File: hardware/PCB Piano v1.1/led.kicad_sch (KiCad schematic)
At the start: 46 parts, among them U4 PCA9685BS, U6 PCA9685BS

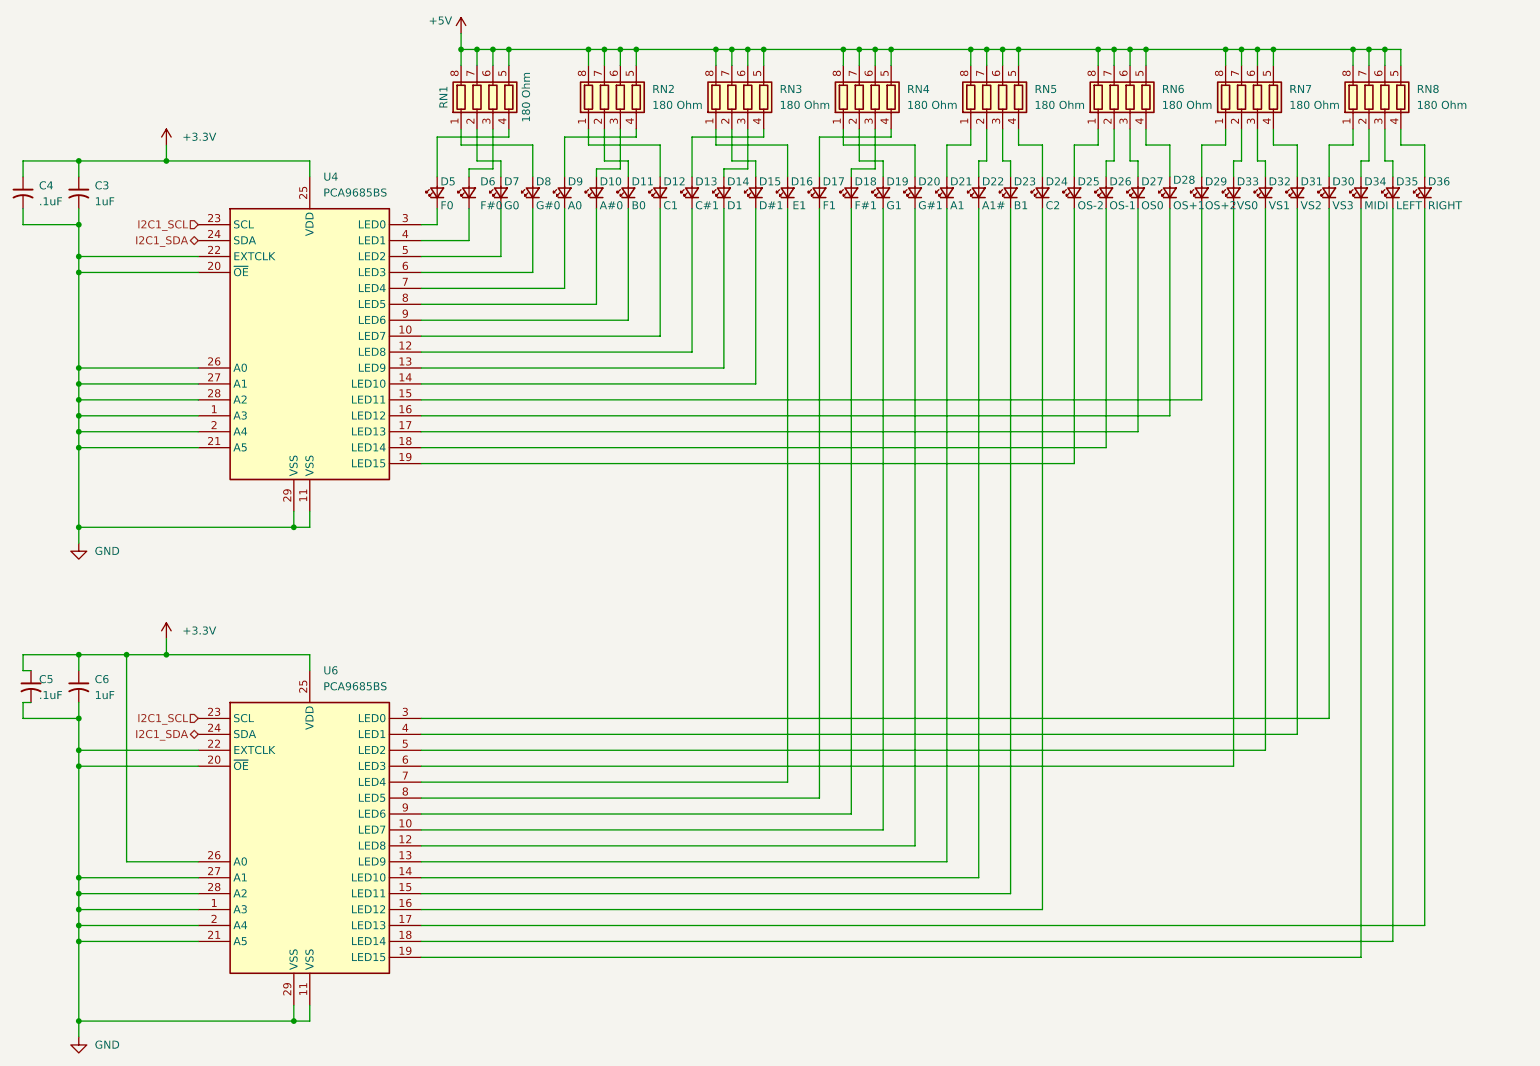
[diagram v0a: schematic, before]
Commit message: Firmware architecture complete - PCB revision with new charger.
Firmware Architecture Complete

- Added MP2724 charger driver
- Added TLV320DAC3100 driver
- Added MTCH2120 touch driver
- Added PCA9685 driver
- Added DotStar driver
- Added rotary encoder driver
- Added touch and LED maps
- Added control/audio/voice managers
- Added audio command queue
- Added Core1 audio architecture
- Added status LED system
- Added LED animation framework

Changes hardware schematic and PCB to accommodate a newer-style USB-C sink battery charger chip and USB data MUX to protect MCU while powered off.
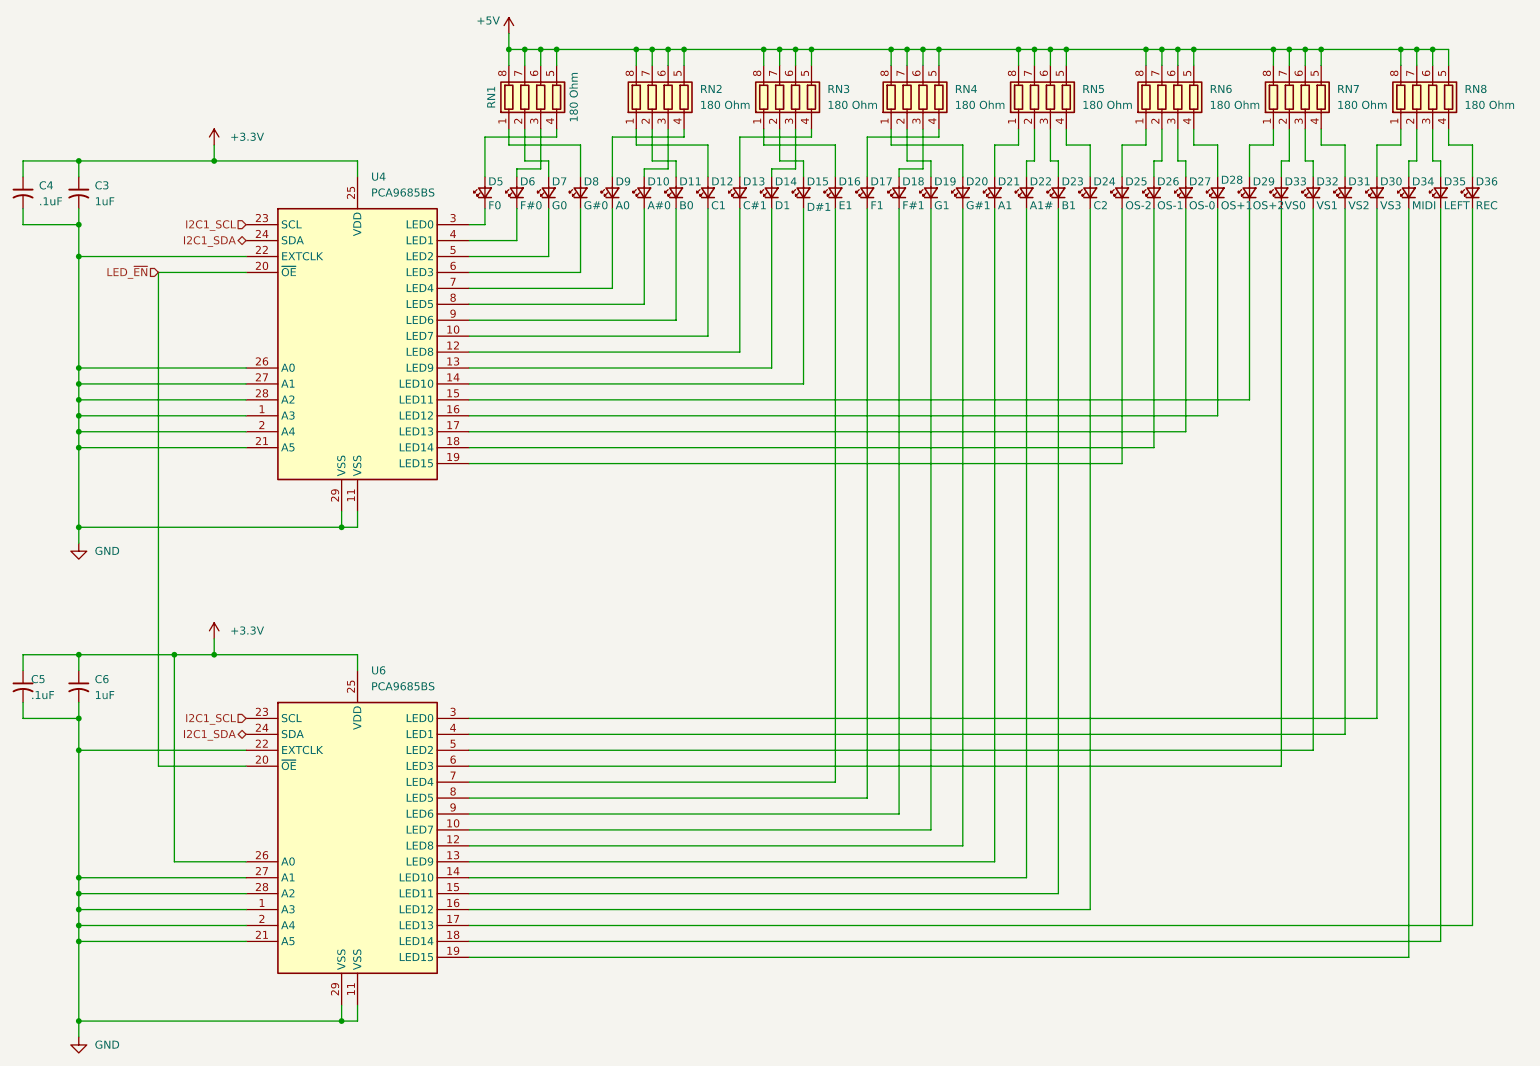
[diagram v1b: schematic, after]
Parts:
- D10: value A#0 -> LTST-C191TBKT; footprint LED_SMD:LED_0603_1608Metric -> PCBPiano_Footprints:LED_0603_1608Metric; Note (none) -> A#0
- D11: value B0 -> LTST-C191TBKT; footprint LED_SMD:LED_0603_1608Metric -> PCBPiano_Footprints:LED_0603_1608Metric; Note (none) -> B0
- D12: value C1 -> LTST-C191TBKT; footprint LED_SMD:LED_0603_1608Metric -> PCBPiano_Footprints:LED_0603_1608Metric; Note (none) -> C1
- D13: value C#1 -> LTST-C191TBKT; footprint LED_SMD:LED_0603_1608Metric -> PCBPiano_Footprints:LED_0603_1608Metric; Note (none) -> C#1
- D14: value D1 -> LTST-C191TBKT; footprint LED_SMD:LED_0603_1608Metric -> PCBPiano_Footprints:LED_0603_1608Metric; Note (none) -> D1
- D15: value D#1 -> LTST-C191TBKT; footprint LED_SMD:LED_0603_1608Metric -> PCBPiano_Footprints:LED_0603_1608Metric; Note (none) -> D#1
- D16: value E1 -> LTST-C191TBKT; footprint LED_SMD:LED_0603_1608Metric -> PCBPiano_Footprints:LED_0603_1608Metric; Note (none) -> E1
- D17: value F1 -> LTST-C191TBKT; footprint LED_SMD:LED_0603_1608Metric -> PCBPiano_Footprints:LED_0603_1608Metric; Note (none) -> F1
- D18: value F#1 -> LTST-C191TBKT; footprint LED_SMD:LED_0603_1608Metric -> PCBPiano_Footprints:LED_0603_1608Metric; Note (none) -> F#1
- D19: value G1 -> LTST-C191TBKT; footprint LED_SMD:LED_0603_1608Metric -> PCBPiano_Footprints:LED_0603_1608Metric; Note (none) -> G1
- D20: value G#1 -> LTST-C191TBKT; footprint LED_SMD:LED_0603_1608Metric -> PCBPiano_Footprints:LED_0603_1608Metric; Note (none) -> G#1
- D21: value A1 -> LTST-C191TBKT; footprint LED_SMD:LED_0603_1608Metric -> PCBPiano_Footprints:LED_0603_1608Metric; Note (none) -> A1
- D22: value A1# -> LTST-C191TBKT; footprint LED_SMD:LED_0603_1608Metric -> PCBPiano_Footprints:LED_0603_1608Metric; Note (none) -> A1#
- D23: value B1 -> LTST-C191TBKT; footprint LED_SMD:LED_0603_1608Metric -> PCBPiano_Footprints:LED_0603_1608Metric; Note (none) -> B1
- D24: value C2 -> LTST-C191TBKT; footprint LED_SMD:LED_0603_1608Metric -> PCBPiano_Footprints:LED_0603_1608Metric; Note (none) -> C2
- D25: value OS-2 -> LTST-C191TBKT; footprint LED_SMD:LED_0603_1608Metric -> PCBPiano_Footprints:LED_0603_1608Metric; Purpose (none) -> OS-2
- D26: value OS-1 -> LTST-C191TBKT; footprint LED_SMD:LED_0603_1608Metric -> PCBPiano_Footprints:LED_0603_1608Metric; Purpose (none) -> OS-1
- D27: value OS0 -> LTST-C191TBKT; footprint LED_SMD:LED_0603_1608Metric -> PCBPiano_Footprints:LED_0603_1608Metric; Purpose (none) -> OS-0
- D28: value OS+1 -> LTST-C191TBKT; footprint LED_SMD:LED_0603_1608Metric -> PCBPiano_Footprints:LED_0603_1608Metric; Purpose (none) -> OS+1
- D29: value OS+2 -> LTST-C191TBKT; footprint LED_SMD:LED_0603_1608Metric -> PCBPiano_Footprints:LED_0603_1608Metric; Purpose (none) -> OS+2
- D30: value VS3 -> LTST-C191TBKT; footprint LED_SMD:LED_0603_1608Metric -> PCBPiano_Footprints:LED_0603_1608Metric; Purpose (none) -> VS3
- D31: value VS2 -> LTST-C191TBKT; footprint LED_SMD:LED_0603_1608Metric -> PCBPiano_Footprints:LED_0603_1608Metric; Purpose (none) -> VS2
- D32: value VS1 -> LTST-C191TBKT; footprint LED_SMD:LED_0603_1608Metric -> PCBPiano_Footprints:LED_0603_1608Metric; Purpose (none) -> VS1
- D33: value VS0 -> LTST-C191TBKT; footprint LED_SMD:LED_0603_1608Metric -> PCBPiano_Footprints:LED_0603_1608Metric; Purpose (none) -> VS0
- D34: value MIDI -> LTST-C191TBKT; footprint LED_SMD:LED_0603_1608Metric -> PCBPiano_Footprints:LED_0603_1608Metric; Purpose (none) -> MIDI
- D35: value LEFT -> LTST-C191TBKT; footprint LED_SMD:LED_0603_1608Metric -> PCBPiano_Footprints:LED_0603_1608Metric; Purpose (none) -> LEFT
- D36: value RIGHT -> LTST-C191TBKT; footprint LED_SMD:LED_0603_1608Metric -> PCBPiano_Footprints:LED_0603_1608Metric; Purpose (none) -> REC
- D5: value F0 -> LTST-C191TBKT; footprint LED_SMD:LED_0603_1608Metric -> PCBPiano_Footprints:LED_0603_1608Metric; Note (none) -> F0
- D6: value F#0 -> LTST-C191TBKT; footprint LED_SMD:LED_0603_1608Metric -> PCBPiano_Footprints:LED_0603_1608Metric; Note (none) -> F#0
- D7: value G0 -> LTST-C191TBKT; footprint LED_SMD:LED_0603_1608Metric -> PCBPiano_Footprints:LED_0603_1608Metric; Note (none) -> G0
- D8: value G#0 -> LTST-C191TBKT; footprint LED_SMD:LED_0603_1608Metric -> PCBPiano_Footprints:LED_0603_1608Metric; Note (none) -> G#0
- D9: value A0 -> LTST-C191TBKT; footprint LED_SMD:LED_0603_1608Metric -> PCBPiano_Footprints:LED_0603_1608Metric; Note (none) -> A0
- RN1, RN2, RN3, RN4, RN5, RN6, RN7, RN8: footprint Resistor_SMD:R_Array_Convex_4x1206 -> PCBPiano_Footprints:R_Array_Convex_4x1206
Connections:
- net GND: no longer U4.20 (~{OE}), U6.20 (~{OE})
- new net LED_~{EN}: U4.20 (~{OE}), U6.20 (~{OE})
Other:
- moved on the sheet: C5, D10, D11, D12, D13, D14, D15, D16, D17, D18, D19, D20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

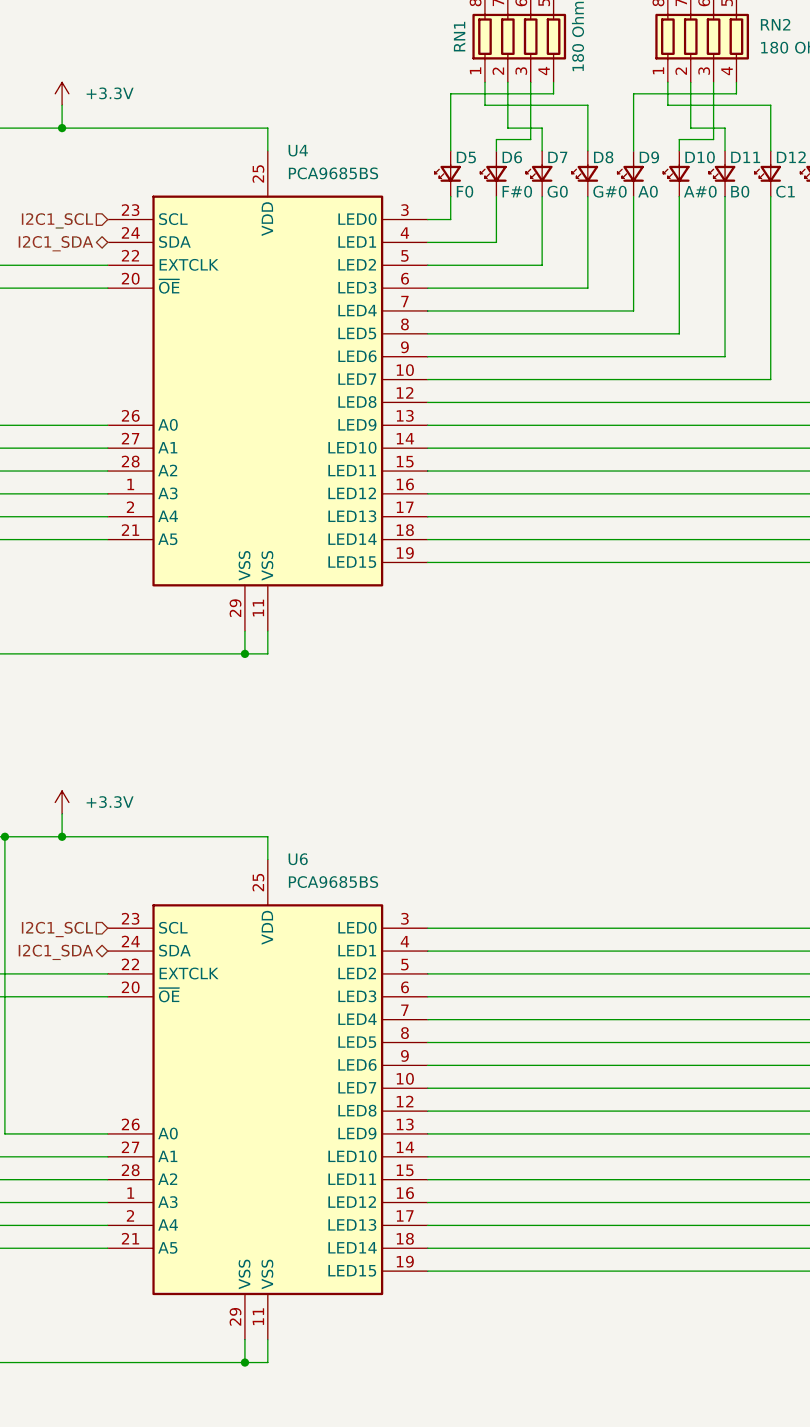
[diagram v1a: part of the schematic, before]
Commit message: PCB Finalized and Ordered. Firmware near completion.
PCB Finalized and Ordered. Final revisions included fixing bugs on some peripheral chips. Also added an RTC circuit after realizing the SD card could benefit from adding file timestamps.

Firmware near completion. Still need to finalize some SD card operations. Synth audio core is finished and all the board peripheral chip drivers were completed.
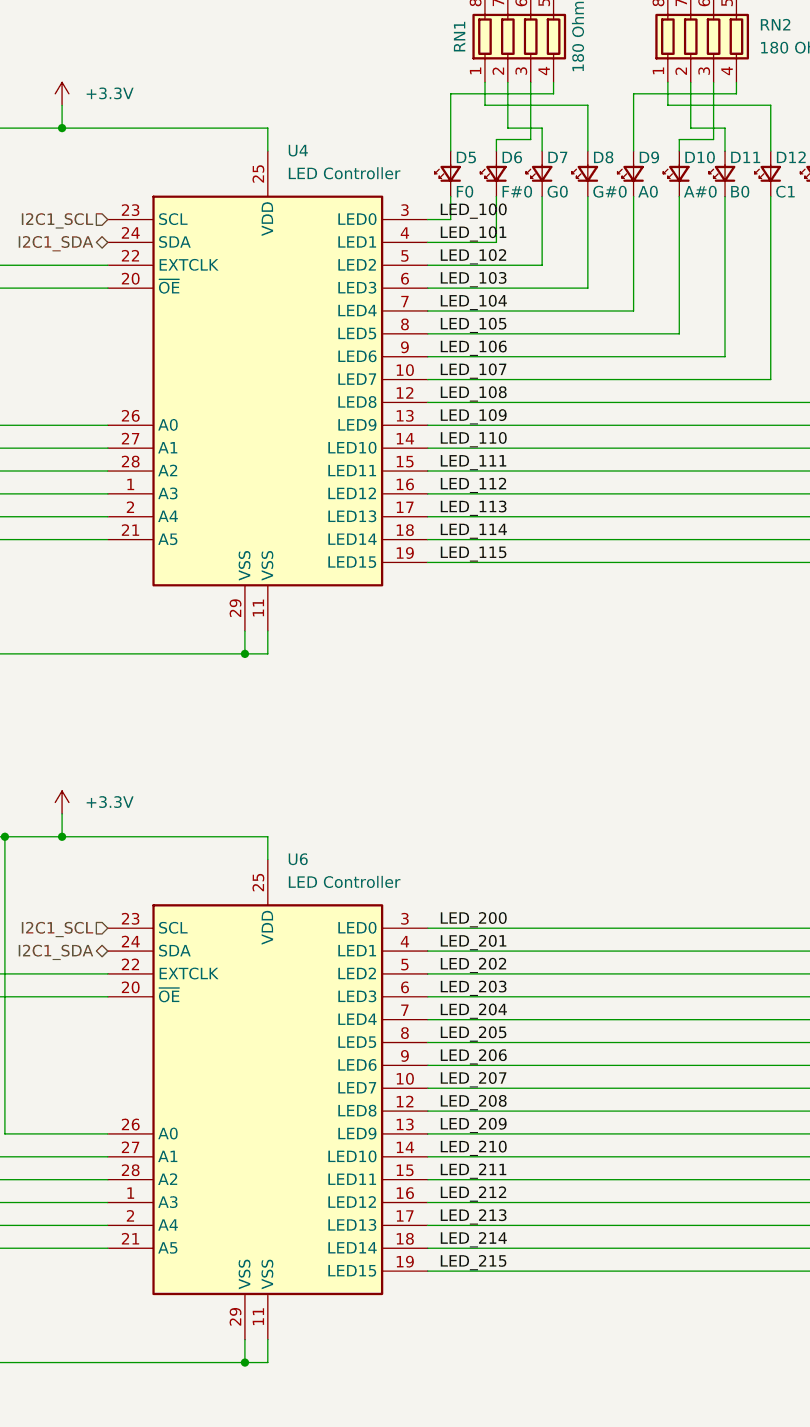
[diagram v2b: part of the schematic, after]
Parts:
- C3, C6: DigiKey_Part_Number (none) -> 1276-1184-1-ND; Manufacturer Part Number (none) -> CL10B105KA8NNNC; Volt Rating (none) -> 10V
- C4, C5: DigiKey_Part_Number (none) -> 1276-1935-2-ND; Manufacturer Part Number (none) -> CL10B104KB8NNWC; Volt Rating (none) -> 10V
- D10, D11, D12, D13, D14, D15, D16, D17, D18, D19, D20, D21, D22, D23, D24, D25, D26, D27, D28, D29, D30, D31, D32, D33, D34, D35, D36, D5, D6, D7, D8, D9: value LTST-C191TBKT -> 3.3Vf, 104mcd; DigiKey_Part_Number (none) -> LTST-C191TBKT; Manufacturer Part Number (none) -> LTST-C191TBKT
- RN1, RN2, RN3, RN4, RN5, RN6, RN7, RN8: Volt Rating (none) -> 6V, 1/10W
- U4, U6: value PCA9685BS -> LED Controller; DigiKey_Part_Number (none) -> PCA9685BS; Manufacturer Part Number (none) -> PCA9685BS
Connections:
- net LED_100: now reaches D5.1 (K), U4.3 (LED0)
- net LED_108: now reaches D13.1 (K), U4.12 (LED8)
- net LED_207: now reaches D19.1 (K), U6.10 (LED7)
- net LED_208: now reaches D20.1 (K), U6.12 (LED8)
- net LED_209: now reaches D21.1 (K), U6.13 (LED9)
- net LED_210: now reaches D22.1 (K), U6.14 (LED10)
- net LED_211: now reaches D23.1 (K), U6.15 (LED11)
- net LED_212: now reaches D24.1 (K), U6.16 (LED12)
- net LED_213: now reaches D36.1 (K), U6.17 (LED13)
- net LED_214: now reaches D35.1 (K), U6.18 (LED14)
- net LED_215: now reaches D34.1 (K), U6.19 (LED15)
- net LED_200: now reaches D30.1 (K), U6.3 (LED0)
- net LED_201: now reaches D31.1 (K), U6.4 (LED1)
- net LED_202: now reaches D32.1 (K), U6.5 (LED2)
- net LED_203: now reaches D33.1 (K), U6.6 (LED3)
- net LED_204: now reaches D16.1 (K), U6.7 (LED4)
- net LED_205: now reaches D17.1 (K), U6.8 (LED5)
- net LED_206: now reaches D18.1 (K), U6.9 (LED6)
- net LED_107: now reaches D12.1 (K), U4.10 (LED7)
- net LED_109: now reaches D14.1 (K), U4.13 (LED9)
- net LED_110: now reaches D15.1 (K), U4.14 (LED10)
- net LED_111: now reaches D29.1 (K), U4.15 (LED11)
- net LED_112: now reaches D28.1 (K), U4.16 (LED12)
- net LED_113: now reaches D27.1 (K), U4.17 (LED13)
- net LED_114: now reaches D26.1 (K), U4.18 (LED14)
- net LED_115: now reaches D25.1 (K), U4.19 (LED15)
- net LED_101: now reaches D6.1 (K), U4.4 (LED1)
- net LED_102: now reaches D7.1 (K), U4.5 (LED2)
- net LED_103: now reaches D8.1 (K), U4.6 (LED3)
- net LED_104: now reaches D9.1 (K), U4.7 (LED4)
- net LED_105: now reaches D10.1 (K), U4.8 (LED5)
- net LED_106: now reaches D11.1 (K), U4.9 (LED6)
